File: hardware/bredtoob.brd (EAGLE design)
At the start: 203.2 x 203.2 mm, 63 parts

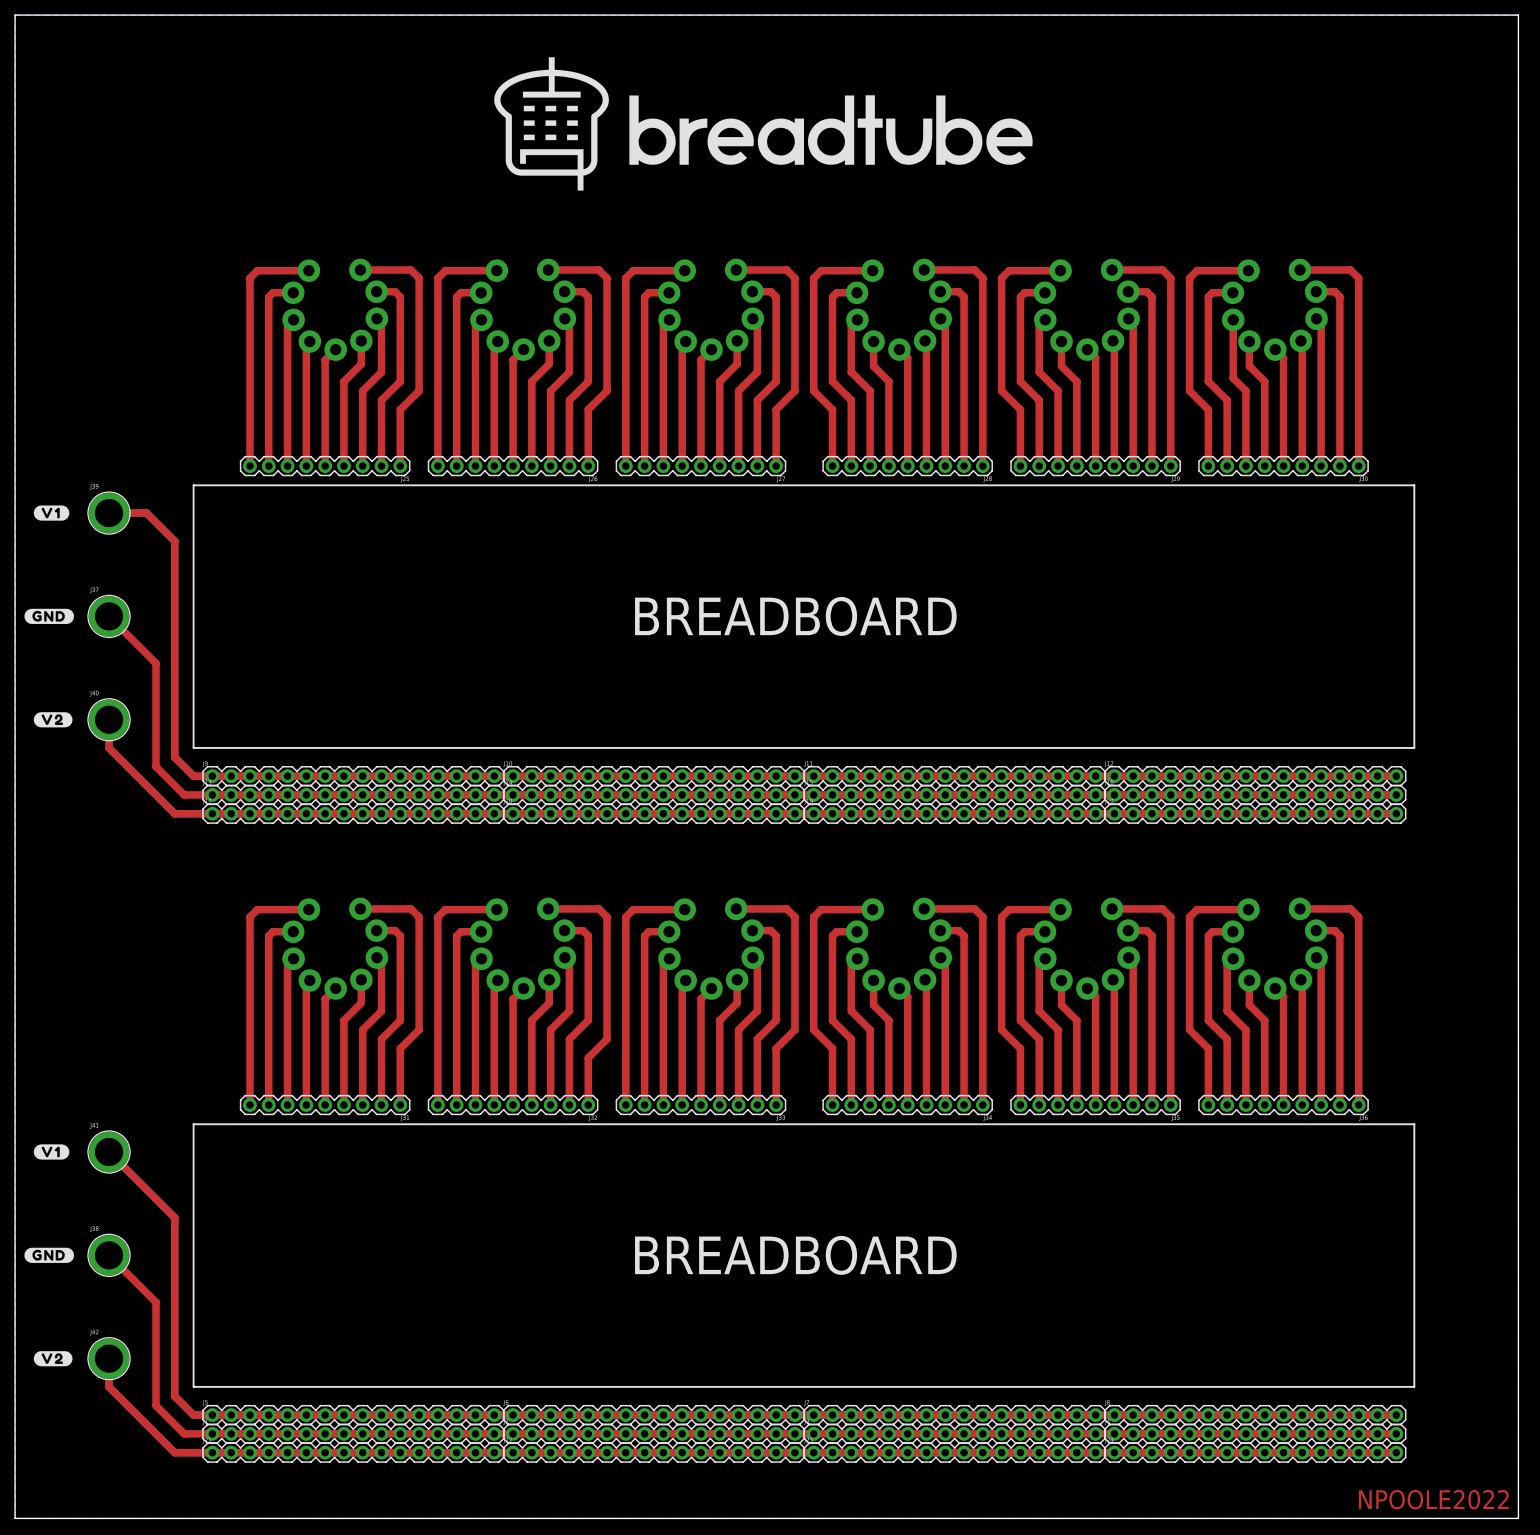
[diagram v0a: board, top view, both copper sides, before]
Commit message: v02
Swap half the noval tube sockets for b7g sockets so we support almost all miniature tubes (compactrons notwithstanding)

Radius the corners of the board

Reduce rails to 40 pins to match common header strips

Add bus headers beside each breadboard to reduce mess if you need to wire between the two
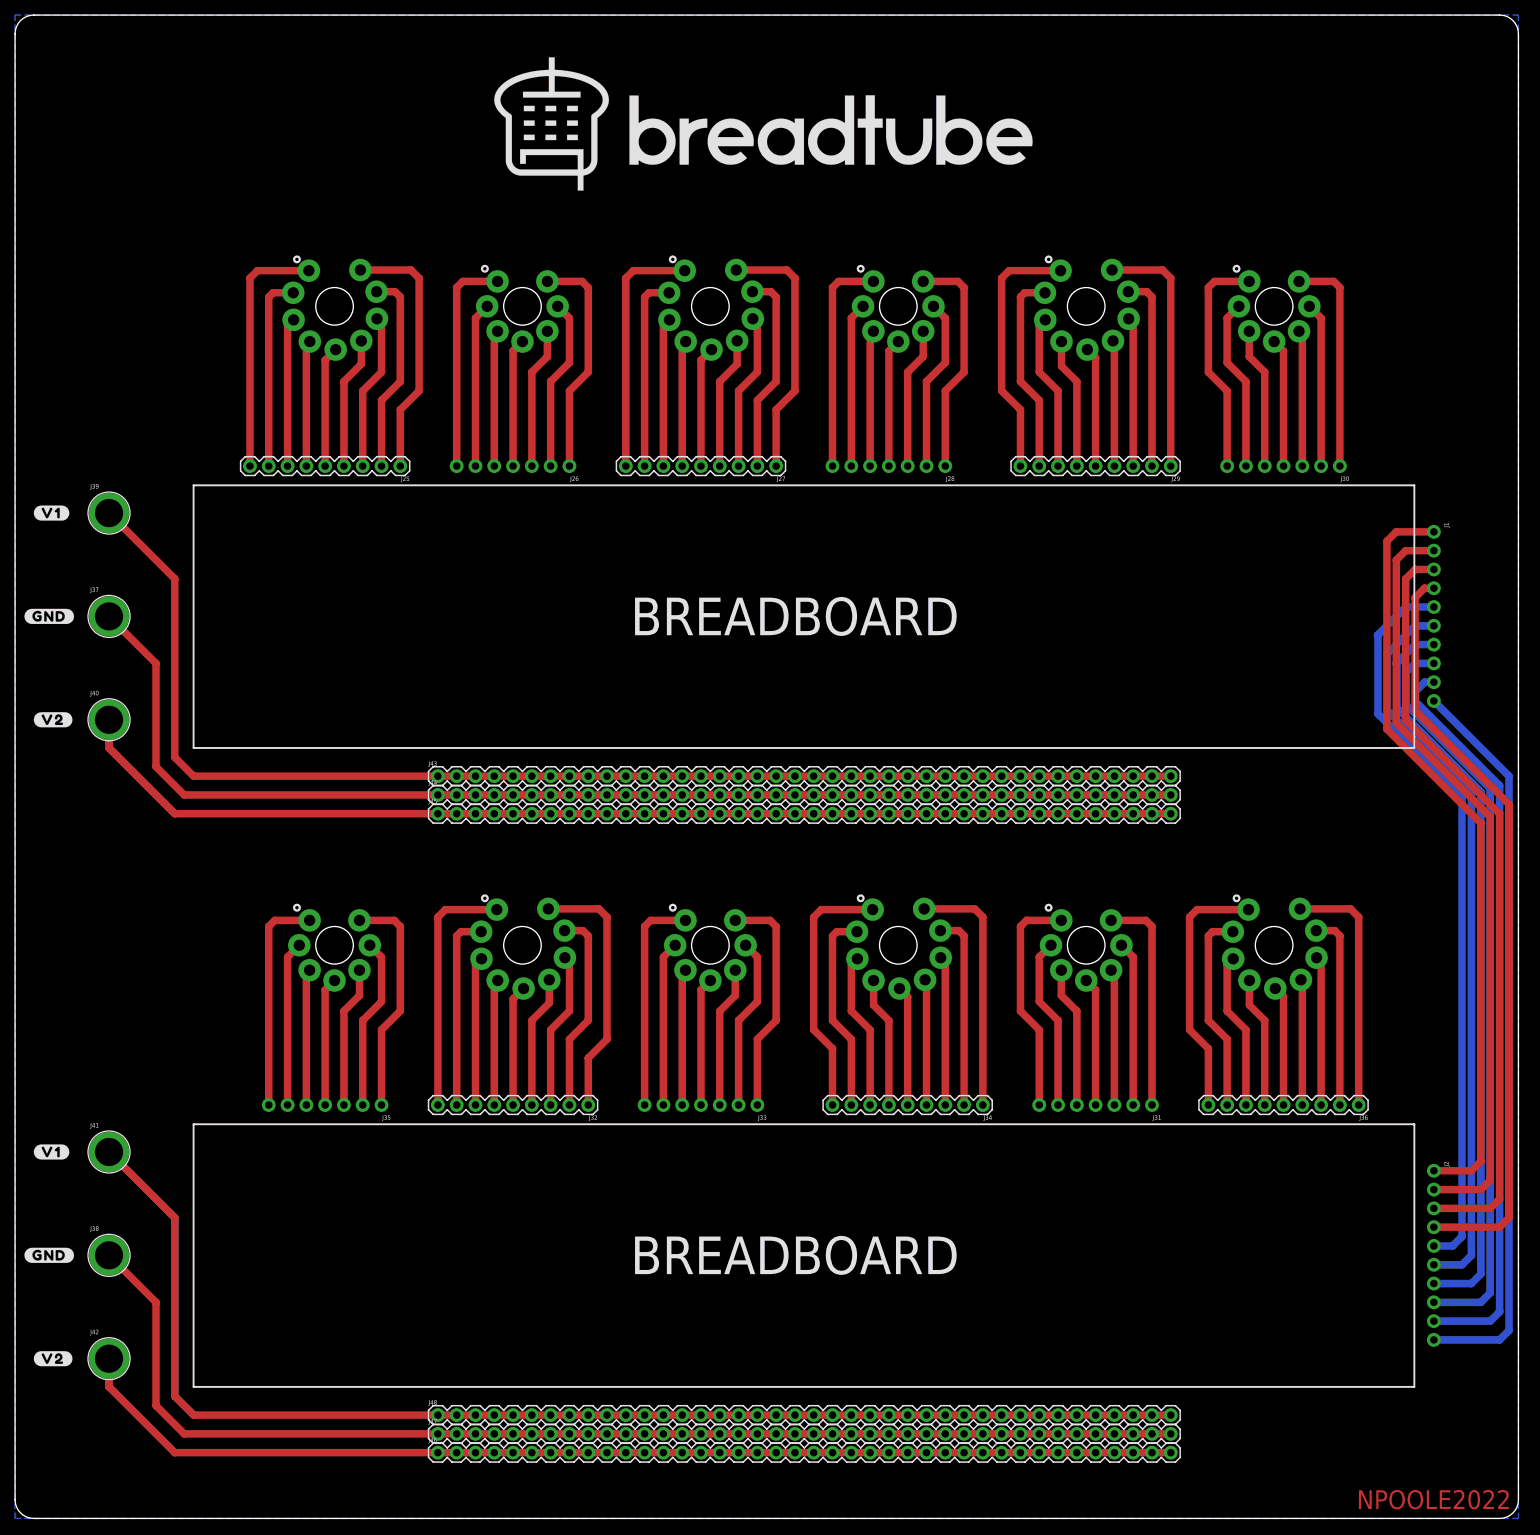
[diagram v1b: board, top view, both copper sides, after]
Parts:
- removed J10, J11, J12, J13, J14, J15, J16, J17, J18, J19, J20, J21, J22, J23, J24, J3, J4, J5, J6, J7, J8, J9: (no value), SparkFun-Connectors:1X16
- added J43, J44, J45, J46, J47, J48: (no value), SparkFun-Connectors:1X40
- J1, J2: device SparkFun-Connectors:1X16 -> SparkFun-Connectors:1X10_NO_SILK
- J26, J28, J30, J31, J33, J35: device SparkFun-Connectors:1X09 -> SparkFun-Connectors:1X07_NO_SILK
- U$11, U$2, U$4, U$6, U$7, U$9: value 9PINMINI -> 7PINMINI; device Toob:9-PIN-MINIATURE -> Toob:7-PIN-MINIATURE(B7G)
- moved J1 205.2 mm to (191.8, 133.3), turned to 270 degrees
- moved J2 129.4 mm to (191.8, 47.0), turned to 270 degrees
- moved J35 106.7 mm to (49.5, 55.9)
- moved J31 101.6 mm to (153.7, 55.9)
- moved J28 5.08 mm to (125.7, 142.2)
- moved J30 2.54 mm to (179.1, 142.2)
- moved J33 2.54 mm to (100.3, 55.9)
- moved J26 2.54 mm to (74.9, 142.2)
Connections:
- removed net N$105: J35.1, U$11.PIN9
- removed net N$16: J26.9, U$2.PIN1
- removed net N$24: J26.1, U$2.PIN9
- removed net N$34: J28.9, U$4.PIN1
- removed net N$42: J28.1, U$4.PIN9
- removed net N$52: J30.9, U$6.PIN1
- removed net N$60: J30.1, U$6.PIN9
- removed net N$61: J31.9, U$7.PIN1
- removed net N$69: J31.1, U$7.PIN9
- removed net N$79: J33.9, U$9.PIN1
- removed net N$87: J33.1, U$9.PIN9
- removed net N$97: J35.9, U$11.PIN1
- new net A: J1.1, J2.1
- new net B: J1.2, J2.2
- new net C: J1.3, J2.3
- new net D: J1.4, J2.4
- new net E: J1.5, J2.5
- new net F: J1.6, J2.6
- new net G: J1.7, J2.7
- new net H: J1.8, J2.8
- new net I: J1.9, J2.9
- new net J: J1.10, J2.10
- net GND: now also J44.1, J44.10, J44.11, J44.12, J44.13, J44.14, J44.15, J44.16, J44.17, J44.18, J44.19, J44.2, J44.20, J44.21, J44.22, J44.23, J44.24, J44.25, J44.26, J44.27, J44.28, J44.29, J44.3, J44.30, J44.31, J44.32, J44.33, J44.34, J44.35, J44.36, J44.37, J44.38, J44.39, J44.4, J44.40, J44.5, J44.6, J44.7, J44.8, J44.9, J47.1, J47.10, J47.11, J47.12, J47.13, J47.14, J47.15, J47.16, J47.17, J47.18, J47.19, J47.2, J47.20, J47.21, J47.22, J47.23, J47.24, J47.25, J47.26, J47.27, J47.28, J47.29, J47.3, J47.30, J47.31, J47.32, J47.33, J47.34, J47.35, J47.36, J47.37, J47.38, J47.39, J47.4, J47.40, J47.5, J47.6, J47.7, J47.8, J47.9; no longer J1.1, J1.10, J1.11, J1.12, J1.13, J1.14, J1.15, J1.16, J1.2, J1.3, J1.4, J1.5, J1.6, J1.7, J1.8, J1.9, J13.1, J13.10, J13.11, J13.12, J13.13, J13.14, J13.15, J13.16, J13.2, J13.3, J13.4, J13.5, J13.6, J13.7, J13.8, J13.9, J14.1, J14.10, J14.11, J14.12, J14.13, J14.14, J14.15, J14.16, J14.2, J14.3, J14.4, J14.5, J14.6, J14.7, J14.8, J14.9, J15.1, J15.10, J15.11, J15.12, J15.13, J15.14, J15.15, J15.16, J15.2, J15.3, J15.4, J15.5, J15.6, J15.7, J15.8, J15.9, J16.1, J16.10, J16.11, J16.12, J16.13, J16.14, J16.15, J16.16, J16.2, J16.3, J16.4, J16.5, J16.6, J16.7, J16.8, J16.9, J2.1, J2.10, J2.11, J2.12, J2.13, J2.14, J2.15, J2.16, J2.2, J2.3, J2.4, J2.5, J2.6, J2.7, J2.8, J2.9, J3.1, J3.10, J3.11, J3.12, J3.13, J3.14, J3.15, J3.16, J3.2, J3.3, J3.4, J3.5, J3.6, J3.7, J3.8, J3.9, J4.1, J4.10, J4.11, J4.12, J4.13, J4.14, J4.15, J4.16, J4.2, J4.3, J4.4, J4.5, J4.6, J4.7, J4.8, J4.9
- net N$1: now also J43.1, J43.10, J43.11, J43.12, J43.13, J43.14, J43.15, J43.16, J43.17, J43.18, J43.19, J43.2, J43.20, J43.21, J43.22, J43.23, J43.24, J43.25, J43.26, J43.27, J43.28, J43.29, J43.3, J43.30, J43.31, J43.32, J43.33, J43.34, J43.35, J43.36, J43.37, J43.38, J43.39, J43.4, J43.40, J43.5, J43.6, J43.7, J43.8, J43.9; no longer J10.1, J10.10, J10.11, J10.12, J10.13, J10.14, J10.15, J10.16, J10.2, J10.3, J10.4, J10.5, J10.6, J10.7, J10.8, J10.9, J11.1, J11.10, J11.11, J11.12, J11.13, J11.14, J11.15, J11.16, J11.2, J11.3, J11.4, J11.5, J11.6, J11.7, J11.8, J11.9, J12.1, J12.10, J12.11, J12.12, J12.13, J12.14, J12.15, J12.16, J12.2, J12.3, J12.4, J12.5, J12.6, J12.7, J12.8, J12.9, J9.1, J9.10, J9.11, J9.12, J9.13, J9.14, J9.15, J9.16, J9.2, J9.3, J9.4, J9.5, J9.6, J9.7, J9.8, J9.9
- net N$100: now also J31.5, U$11.3; no longer J35.6, U$11.PIN4
- net N$101: now also J31.4, U$11.4; no longer J35.5, U$11.PIN5
- net N$102: now also J31.3, U$11.5; no longer J35.4, U$11.PIN6
- net N$103: now also J31.2, U$11.6; no longer J35.3, U$11.PIN7
- net N$104: now also J31.1, U$11.7; no longer J35.2, U$11.PIN8
- net N$17: now also J26.7, U$2.1; no longer J26.8, U$2.PIN2
- net N$18: now also J26.6, U$2.2; no longer J26.7, U$2.PIN3
- net N$19: now also J26.5, U$2.3; no longer J26.6, U$2.PIN4
- net N$2: now also J45.1, J45.10, J45.11, J45.12, J45.13, J45.14, J45.15, J45.16, J45.17, J45.18, J45.19, J45.2, J45.20, J45.21, J45.22, J45.23, J45.24, J45.25, J45.26, J45.27, J45.28, J45.29, J45.3, J45.30, J45.31, J45.32, J45.33, J45.34, J45.35, J45.36, J45.37, J45.38, J45.39, J45.4, J45.40, J45.5, J45.6, J45.7, J45.8, J45.9; no longer J17.1, J17.10, J17.11, J17.12, J17.13, J17.14, J17.15, J17.16, J17.2, J17.3, J17.4, J17.5, J17.6, J17.7, J17.8, J17.9, J18.1, J18.10, J18.11, J18.12, J18.13, J18.14, J18.15, J18.16, J18.2, J18.3, J18.4, J18.5, J18.6, J18.7, J18.8, J18.9, J19.1, J19.10, J19.11, J19.12, J19.13, J19.14, J19.15, J19.16, J19.2, J19.3, J19.4, J19.5, J19.6, J19.7, J19.8, J19.9, J20.1, J20.10, J20.11, J20.12, J20.13, J20.14, J20.15, J20.16, J20.2, J20.3, J20.4, J20.5, J20.6, J20.7, J20.8, J20.9
- net N$20: now also J26.4, U$2.4; no longer J26.5, U$2.PIN5
- net N$21: now also J26.3, U$2.5; no longer J26.4, U$2.PIN6
- net N$22: now also J26.2, U$2.6; no longer J26.3, U$2.PIN7
- net N$23: now also J26.1, U$2.7; no longer J26.2, U$2.PIN8
- net N$3: now also J46.1, J46.10, J46.11, J46.12, J46.13, J46.14, J46.15, J46.16, J46.17, J46.18, J46.19, J46.2, J46.20, J46.21, J46.22, J46.23, J46.24, J46.25, J46.26, J46.27, J46.28, J46.29, J46.3, J46.30, J46.31, J46.32, J46.33, J46.34, J46.35, J46.36, J46.37, J46.38, J46.39, J46.4, J46.40, J46.5, J46.6, J46.7, J46.8, J46.9; no longer J21.1, J21.10, J21.11, J21.12, J21.13, J21.14, J21.15, J21.16, J21.2, J21.3, J21.4, J21.5, J21.6, J21.7, J21.8, J21.9, J22.1, J22.10, J22.11, J22.12, J22.13, J22.14, J22.15, J22.16, J22.2, J22.3, J22.4, J22.5, J22.6, J22.7, J22.8, J22.9, J23.1, J23.10, J23.11, J23.12, J23.13, J23.14, J23.15, J23.16, J23.2, J23.3, J23.4, J23.5, J23.6, J23.7, J23.8, J23.9, J24.1, J24.10, J24.11, J24.12, J24.13, J24.14, J24.15, J24.16, J24.2, J24.3, J24.4, J24.5, J24.6, J24.7, J24.8, J24.9
- net N$35: now also J28.7, U$4.1; no longer J28.8, U$4.PIN2
- net N$36: now also J28.6, U$4.2; no longer J28.7, U$4.PIN3
- net N$37: now also J28.5, U$4.3; no longer J28.6, U$4.PIN4
- net N$38: now also J28.4, U$4.4; no longer J28.5, U$4.PIN5
- net N$39: now also J28.3, U$4.5; no longer J28.4, U$4.PIN6
- net N$4: now also J48.1, J48.10, J48.11, J48.12, J48.13, J48.14, J48.15, J48.16, J48.17, J48.18, J48.19, J48.2, J48.20, J48.21, J48.22, J48.23, J48.24, J48.25, J48.26, J48.27, J48.28, J48.29, J48.3, J48.30, J48.31, J48.32, J48.33, J48.34, J48.35, J48.36, J48.37, J48.38, J48.39, J48.4, J48.40, J48.5, J48.6, J48.7, J48.8, J48.9; no longer J5.1, J5.10, J5.11, J5.12, J5.13, J5.14, J5.15, J5.16, J5.2, J5.3, J5.4, J5.5, J5.6, J5.7, J5.8, J5.9, J6.1, J6.10, J6.11, J6.12, J6.13, J6.14, J6.15, J6.16, J6.2, J6.3, J6.4, J6.5, J6.6, J6.7, J6.8, J6.9, J7.1, J7.10, J7.11, J7.12, J7.13, J7.14, J7.15, J7.16, J7.2, J7.3, J7.4, J7.5, J7.6, J7.7, J7.8, J7.9, J8.1, J8.10, J8.11, J8.12, J8.13, J8.14, J8.15, J8.16, J8.2, J8.3, J8.4, J8.5, J8.6, J8.7, J8.8, J8.9
- net N$40: now also J28.2, U$4.6; no longer J28.3, U$4.PIN7
- net N$41: now also J28.1, U$4.7; no longer J28.2, U$4.PIN8
- net N$53: now also J30.7, U$6.1; no longer J30.8, U$6.PIN2
- net N$54: now also J30.6, U$6.2; no longer J30.7, U$6.PIN3
- net N$55: now also J30.5, U$6.3; no longer J30.6, U$6.PIN4
- net N$56: now also J30.4, U$6.4; no longer J30.5, U$6.PIN5
- net N$57: now also J30.3, U$6.5; no longer J30.4, U$6.PIN6
- net N$58: now also J30.2, U$6.6; no longer J30.3, U$6.PIN7
- net N$59: now also J30.1, U$6.7; no longer J30.2, U$6.PIN8
- net N$62: now also J35.7, U$7.1; no longer J31.8, U$7.PIN2
- net N$63: now also J35.6, U$7.2; no longer J31.7, U$7.PIN3
- net N$64: now also J35.5, U$7.3; no longer J31.6, U$7.PIN4
- net N$65: now also J35.4, U$7.4; no longer J31.5, U$7.PIN5
- net N$66: now also J35.3, U$7.5; no longer J31.4, U$7.PIN6
- net N$67: now also J35.2, U$7.6; no longer J31.3, U$7.PIN7
- net N$68: now also J35.1, U$7.7; no longer J31.2, U$7.PIN8
- net N$80: now also J33.7, U$9.1; no longer J33.8, U$9.PIN2
- net N$81: now also J33.6, U$9.2; no longer J33.7, U$9.PIN3
- net N$82: now also J33.5, U$9.3; no longer J33.6, U$9.PIN4
- net N$83: now also J33.4, U$9.4; no longer J33.5, U$9.PIN5
- net N$84: now also J33.3, U$9.5; no longer J33.4, U$9.PIN6
- net N$85: now also J33.2, U$9.6; no longer J33.3, U$9.PIN7
- net N$86: now also J33.1, U$9.7; no longer J33.2, U$9.PIN8
- net N$98: now also J31.7, U$11.1; no longer J35.8, U$11.PIN2
- net N$99: now also J31.6, U$11.2; no longer J35.7, U$11.PIN3
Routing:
- net N$1: track 411.7 -> 172.4 mm
- net N$3: track 363.0 -> 167.4 mm
- net N$2: track 363.0 -> 167.4 mm
- net N$4: track 405.7 -> 212.7 mm
- net D: track 0.00 -> 102.8 mm
- net A: track 0.00 -> 102.8 mm
- net C: track 0.00 -> 102.8 mm
- net B: track 0.00 -> 102.8 mm
- net I: track 0.00 -> 101.0 mm
- net H: track 0.00 -> 101.0 mm
- net G: track 0.00 -> 100.3 mm
- net J: track 0.00 -> 100.0 mm
- net F: track 0.00 -> 99.5 mm
- net E: track 0.00 -> 99.5 mm
- net GND: track 384.3 -> 323.4 mm
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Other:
- outline, holes or cut-outs redrawn

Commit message: v03
Glad I waited for parts to come in for testing before ordering v02

- Replace banana jack headers with binding posts
- Widen Pin Receptacle headers to accept Mill-Max 0312-0-15-80-34-80-10-0
- Revise Silkscreen Labels
- Add OSHW Logo
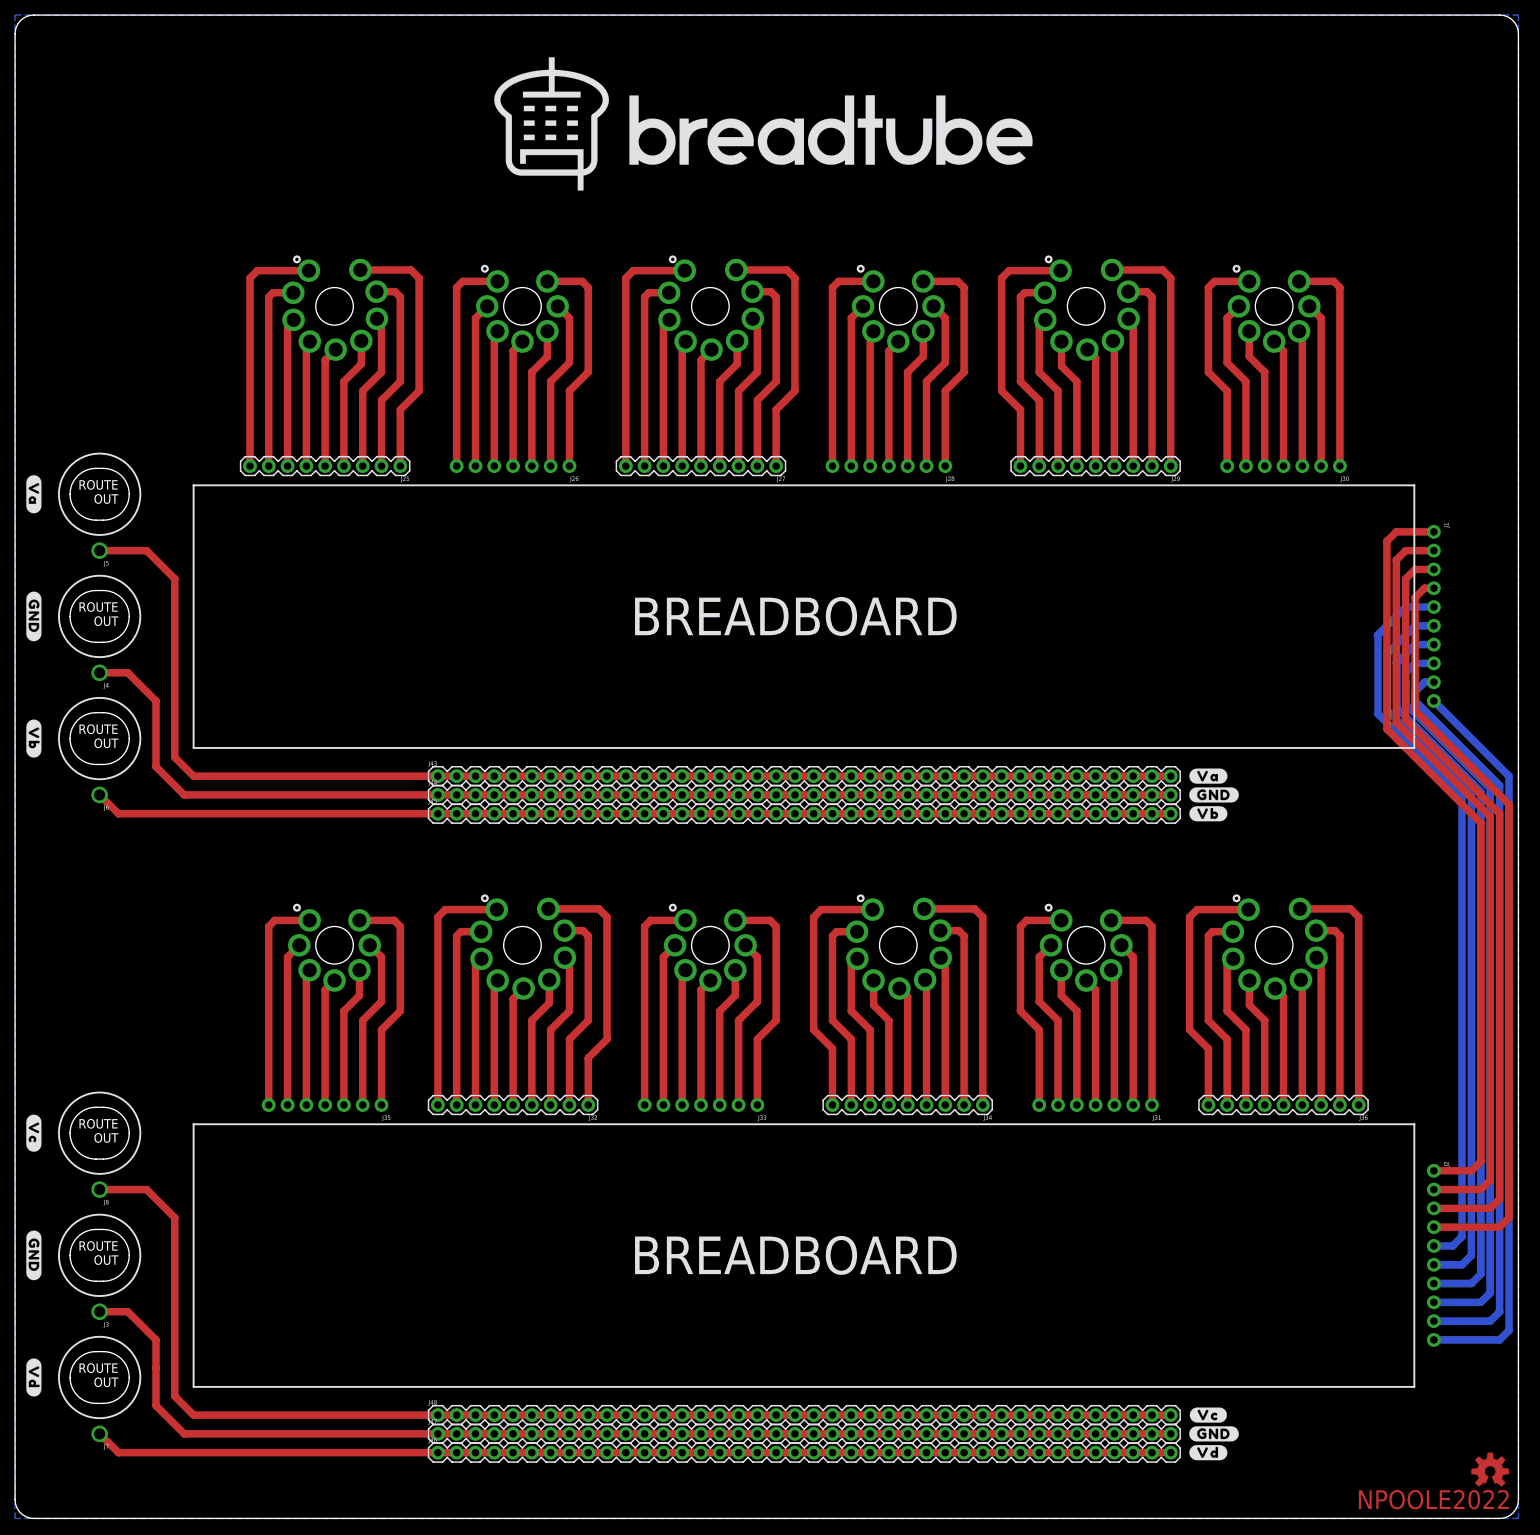
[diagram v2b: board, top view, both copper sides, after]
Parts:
- removed J37, J38, J39, J40, J41, J42: (no value), SparkFun-Connectors:BANANA_CONN
- added J3, J4, J5, J6, J7, J8: BINDING_POST, SparkFun-Connectors:BINDING_POST
- added U$20, U$21: (no value), output:#GND#0
- added U$22: (no value), output:#VA#0
- added U$23: (no value), output:#VB#0
- added U$24: (no value), output:#VC#0
- added U$25: (no value), output:#VD#0
- added U$26: (no value), SparkFun-Aesthetics:OSHW-LOGO-M_COPPER
- U$16: device output:#V1#0 -> output:#VA#0
- U$17: device output:#V1#0 -> output:#VB#0
- U$18: device output:#V2#0 -> output:#VC#0
- U$19: device output:#V2#0 -> output:#VD#0
- moved U$18 55.9 mm to (2.54, 52.1), turned to 270 degrees
- moved U$17 55.9 mm to (2.54, 105.4), turned to 270 degrees
- moved U$16 2.54 mm to (2.54, 138.4), turned to 270 degrees
- moved U$19 2.54 mm to (2.54, 19.1), turned to 270 degrees
- moved U$14 1.27 mm to (2.54, 121.9), turned to 270 degrees
- moved U$15 1.27 mm to (2.54, 35.6), turned to 270 degrees
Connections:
- net GND: now also J3.P$1, J4.P$1; no longer J37.P$1, J38.P$1
- net N$1: now also J5.P$1; no longer J39.P$1
- net N$2: now also J6.P$1; no longer J40.P$1
- net N$3: now also J7.P$1; no longer J42.P$1
- net N$4: now also J8.P$1; no longer J41.P$1
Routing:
- net N$4: track 212.7 -> 171.5 mm
- net N$3: track 167.4 -> 145.8 mm
- net N$2: track 167.4 -> 145.8 mm
- net GND: track 323.4 -> 313.7 mm
- net N$1: track 172.4 -> 171.5 mm
